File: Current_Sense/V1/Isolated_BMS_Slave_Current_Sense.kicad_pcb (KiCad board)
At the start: 2 copper layers, 107.6 x 62.2 mm, 140 parts, among them J202 649002227222, J301 649006227222, J302 649006227222, J401 Header_Male_Pin_2.54mm_1X2_,_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, J501 Header_Male_Pin_2.54mm_1X6_,_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, J502 Header_Male_Pin_2.54mm_1X3_,_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, SW501 PTS645SM43SMTR92, SW502 PTS645SM43SMTR92, U201 LM4040CYM3-4.1-TR, U202 PGA281AIPWR, U203 ADC141S626CIMM/NOPB, U301 SI8422AB-D-IS, U302 SN65HVD232DR, U401 PQMC3-D12-D15-S, U402 NCP1117LPST33T3G, U403 NCP1117ST50T3G, U404 NCP1117LPST33T3G, U501 STM32F446RE

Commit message: minor fix
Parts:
- added C210: 885012107018, Capacitors:C0805, B.Cu at (128.5, 91.7)
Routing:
- net 5VB: track 143.1 -> 145.7 mm
- net /STM32F446/PA3: track 49.5 -> 50.9 mm
- net /STM32F446/PA2: track 48.3 -> 49.1 mm
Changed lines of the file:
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@@
 (kicad_pcb (version 4) (host pcbnew 4.0.5+dfsg1-4)
   (general
-    (links 273)
+    (links 275)
     (no_connects 0)
-    (area 103.048999 60.884999 210.768001 123.265001)
+    (area 95.865647 23.000933 221.091788 157.954066)
     (thickness 1.6)
     (drawings 34)
-    (tracks 1007)
+    (tracks 1009)
     (zones 0)
-    (modules 140)
+    (modules 141)
     (nets 113)
   )
@@
   )
   (setup
-    (last_trace_width 0.254)
+    (last_trace_width 0.508)
     (user_trace_width 0.2032)
     (user_trace_width 0.254)
@@
     (visible_elements FFFFFF7F)
     (pcbplotparams
-      (layerselection 0x00030_80000001)
-      (usegerberextensions false)
+      (layerselection 0x010f0_80000001)
+      (usegerberextensions true)
       (excludeedgelayer true)
       (linewidth 0.100000)
       (plotframeref false)
-      (viasonmask false)
+      (viasonmask true)
       (mode 1)
       (useauxorigin false)
@@
       (outputformat 1)
       (mirror false)
-      (drillshape 1)
+      (drillshape 0)
       (scaleselection 1)
-      (outputdirectory ""))
+      (outputdirectory Gerber/))
   )
   (net 0 "")
@@
   (module Capacitors:C0805 (layer B.Cu)
     (at 131.064 91.712 90)
-    (fp_text reference C205 (at 0.78 -2.159 90) (layer B.SilkS)
+    (fp_text reference C205 (at -3.538 -0.127 90) (layer B.SilkS)
       (effects (font (size 1.27 1.27) (thickness 0.2032)) (justify mirror))
     )
@@
     (at 182.499 100.203)
     (fp_text reference F401 (at -0.254 -3.048) (layer F.SilkS)
-      (effects (font (size 1 1) (thickness 0.2032)))
+      (effects (font (size 1.27 1.27) (thickness 0.2032)))
     )
     (fp_text value 39511000440 (at 0 6.096) (layer F.Fab) hide
@@
     (at 151.511 76.581 90)
     (fp_text reference R404 (at 1.524 -2.032 90) (layer F.SilkS)
-      (effects (font (size 1.27 1.27) (thickness 0.254)))
+      (effects (font (size 1.27 1.27) (thickness 0.2032)))
     )
     (fp_text value RC0805JR-07470RL (at 1.73 2.33 90) (layer F.Fab) hide
@@
     (at 146.812 76.581 90)
     (fp_text reference R405 (at 1.397 -2.159 90) (layer F.SilkS)
-      (effects (font (size 1.27 1.27) (thickness 0.254)))
+      (effects (font (size 1.27 1.27) (thickness 0.2032)))
     )
     (fp_text value RC0805JR-07470RL (at 1.73 2.33 90) (layer F.Fab) hide
@@
   (module Connectors:Headers_2.54mm_1X6 (layer F.Cu)
     (at 111.633 96.266 270)
-    (fp_text reference J501 (at 4.14 -3.84 270) (layer F.SilkS)
-      (effects (font (size 2.54 2.54) (thickness 0.254)))
+    (fp_text reference J501 (at 12.446 -2.667 270) (layer F.SilkS)
+      (effects (font (size 1.27 1.27) (thickness 0.2032)))
     )
     (fp_text value Header_Male_Pin_2.54mm_1X6_,_Unshrouded (at -0.17 5.06 270) (layer F.Fab) hide
@@
   (module Connectors:Headers_2.54mm_1X2 (layer F.Cu)
     (at 149.352 66.04 270)
-    (fp_text reference J401 (at 3.38 -3.3 270) (layer F.SilkS)
-      (effects (font (size 2.54 2.54) (thickness 0.254)))
+    (fp_text reference J401 (at 3.048 2.54 450) (layer F.SilkS)
+      (effects (font (size 1.27 1.27) (thickness 0.2032)))
     )
     (fp_text value Header_Male_Pin_2.54mm_1X2_,_Unshrouded (at -0.13 5.58 270) (layer F.Fab) hide
@@
     )
   )
+  (module Capacitors:C0805 (layer B.Cu)
+    (at 128.524 91.694 90)
+    (fp_text reference C210 (at -3.429 0 90) (layer B.SilkS)
+      (effects (font (size 1.27 1.27) (thickness 0.2032)) (justify mirror))
+    )
+    (fp_text value 885012107018 (at 1.73 -2.33 90) (layer B.Fab) hide
+      (effects (font (size 1.27 1.27) (thickness 0.254)) (justify mirror))
+    )
+    (fp_line (start 0.6 1) (end 1.45 1) (layer B.SilkS) (width 0.254))
+    (fp_line (start 0.6 -1) (end 1.45 -1) (layer B.SilkS) (width 0.254))
+    (pad 1 smd rect (at 0 0 90) (size 1.4 1.5) (layers B.Cu B.Paste B.Mask)
+      (net 5 5VB))
+    (pad 2 smd rect (at 2.05 0 90) (size 1.4 1.5) (layers B.Cu B.Paste B.Mask)
+      (net 1 DGND))
+    (model Capacitors/C0805.wrl
+      (at (xyz 0.04 0.0005 0))
+      (scale (xyz 0.3937 0.3937 0.3937))
+      (rotate (xyz 0 0 0))
+    )
+  )
   (gr_text 3.3V (at 153.416 63.5) (layer F.SilkS)
     (effects (font (size 1.27 1.27) (thickness 0.2032)))
@@
   (segment (start 131.77 78.161) (end 131.699 78.232) (width 0.254) (layer F.Cu) (net 4))
   (via (at 131.699 78.232) (size 1.016) (drill 0.3302) (layers F.Cu B.Cu) (net 4))
+  (segment (start 131.064 91.712) (end 133.586 91.712) (width 0.508) (layer B.Cu) (net 5))
+  (segment (start 133.586 91.712) (end 133.604 91.694) (width 0.508) (layer B.Cu) (net 5))
+  (segment (start 128.524 91.694) (end 130.937 91.694) (width 0.508) (layer B.Cu) (net 5))
+  (segment (start 130.937 91.839) (end 131.064 91.712) (width 0.508) (layer B.Cu) (net 5))
   (segment (start 151.511 74.531) (end 153.525 74.531) (width 0.254) (layer F.Cu) (net 5))
   (segment (start 153.525 74.531) (end 156.21 77.216) (width 0.254) (layer F.Cu) (net 5))
@@
   (segment (start 130.937 93.19259) (end 131.318 93.19259) (width 0.2032) (layer F.Cu) (net 5))
   (segment (start 131.318 93.19259) (end 133.45159 93.19259) (width 0.2032) (layer F.Cu) (net 5))
-  (segment (start 131.064 91.712) (end 133.586 91.712) (width 0.2032) (layer B.Cu) (net 5))
-  (segment (start 133.586 91.712) (end 133.604 91.694) (width 0.2032) (layer B.Cu) (net 5))
   (segment (start 133.604 93.345) (end 133.604 91.694) (width 0.2032) (layer B.Cu) (net 5))
   (segment (start 133.45159 93.19259) (end 133.604 93.345) (width 0.2032) (layer F.Cu) (net 5))
@@
   (segment (start 116.223 91.313) (end 118.981 91.313) (width 0.508) (layer F.Cu) (net 31))
   (segment (start 118.981 91.313) (end 118.999 91.331) (width 0.508) (layer F.Cu) (net 31))
+  (segment (start 148.971 105.791) (end 148.971 108.458) (width 0.2032) (layer F.Cu) (net 32))
+  (segment (start 148.971 108.458) (end 152.908 112.395) (width 0.2032) (layer F.Cu) (net 32))
+  (segment (start 152.908 112.395) (end 152.908 120.269) (width 0.2032) (layer F.Cu) (net 32))
+  (segment (start 152.908 120.269) (end 151.765 121.412) (width 0.2032) (layer F.Cu) (net 32))
+  (segment (start 151.765 121.412) (end 126.873 121.412) (width 0.2032) (layer F.Cu) (net 32))
+  (segment (start 126.873 121.412) (end 125.476 120.015) (width 0.2032) (layer F.Cu) (net 32))
   (segment (start 125.476 120.015) (end 122.936 120.015) (width 0.2032) (layer F.Cu) (net 32))
   (segment (start 122.936 120.015) (end 121.031 120.015) (width 0.2032) (layer F.Cu) (net 32))
   (segment (start 121.031 120.015) (end 122.936 120.015) (width 0.254) (layer B.Cu) (net 32))
   (via (at 122.936 120.015) (size 1.016) (drill 0.3302) (layers F.Cu B.Cu) (net 32))
-  (segment (start 148.971 105.791) (end 148.971 108.458) (width 0.2032) (layer F.Cu) (net 32))
-  (segment (start 148.971 108.458) (end 152.171411 111.658411) (width 0.2032) (layer F.Cu) (net 32))
-  (segment (start 152.171411 111.658411) (end 152.171411 119.735589) (width 0.2032) (layer F.Cu) (net 32))
-  (segment (start 152.171411 119.735589) (end 150.622 121.285) (width 0.2032) (layer F.Cu) (net 32))
-  (segment (start 150.622 121.285) (end 126.746 121.285) (width 0.2032) (layer F.Cu) (net 32))
-  (segment (start 126.746 121.285) (end 125.476 120.015) (width 0.2032) (layer F.Cu) (net 32))
   (segment (start 186.436 78.74) (end 188.087 78.74) (width 0.508) (layer B.Cu) (net 33))
   (segment (start 188.087 78.74) (end 188.341 78.994) (width 0.508) (layer B.Cu) (net 33))
@@
   (segment (start 111.633 91.313) (end 114.173 91.313) (width 0.508) (layer F.Cu) (net 66))
   (segment (start 146.821 107.941) (end 146.821 108.8942) (width 0.2032) (layer F.Cu) (net 67))
-  (segment (start 151.765001 113.838201) (end 151.765001 119.506999) (width 0.2032) (layer F.Cu) (net 67))
-  (segment (start 146.821 108.8942) (end 151.765001 113.838201) (width 0.2032) (layer F.Cu) (net 67))
-  (segment (start 151.765001 119.506999) (end 150.495 120.777) (width 0.2032) (layer F.Cu) (net 67))
-  (segment (start 150.495 120.777) (end 127.254 120.777) (width 0.2032) (layer F.Cu) (net 67))
-  (segment (start 127.254 120.777) (end 123.952 117.475) (width 0.2032) (layer F.Cu) (net 67))
+  (segment (start 146.821 108.8942) (end 152.146 114.2192) (width 0.2032) (layer F.Cu) (net 67))
+  (segment (start 152.146 114.2192) (end 152.146 119.888) (width 0.2032) (layer F.Cu) (net 67))
+  (segment (start 152.146 119.888) (end 151.13 120.904) (width 0.2032) (layer F.Cu) (net 67))
+  (segment (start 151.13 120.904) (end 127.381 120.904) (width 0.2032) (layer F.Cu) (net 67))
+  (segment (start 127.381 120.904) (end 123.952 117.475) (width 0.2032) (layer F.Cu) (net 67))
   (segment (start 123.952 117.475) (end 118.999 117.475) (width 0.2032) (layer F.Cu) (net 67))
   (segment (start 133.302 77.511) (end 137.543 77.511) (width 0.254) (layer F.Cu) (net 72))
@@
     (polygon
       (pts
-        (xy 204.47 75.311) (xy 204.47 60.96) (xy 107.95 60.96) (xy 107.95 123.19) (xy 162.56 123.19)
+        (xy 203.708 75.311) (xy 203.708 60.96) (xy 107.95 60.96) (xy 107.95 123.19) (xy 162.56 123.19)
         (xy 162.56 76.454) (xy 163.83 75.311)
       )

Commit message: Add Eclipse Logo, generate Gerber
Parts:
- added G***: LOGO, Logo:Eclipse_logo_small, B.Cu at (123.0, 68.5)
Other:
- board text added: "Christian Daigneault-St-Arnaud (c) 2017 - Eclipse X BMS - Current Sense V1"

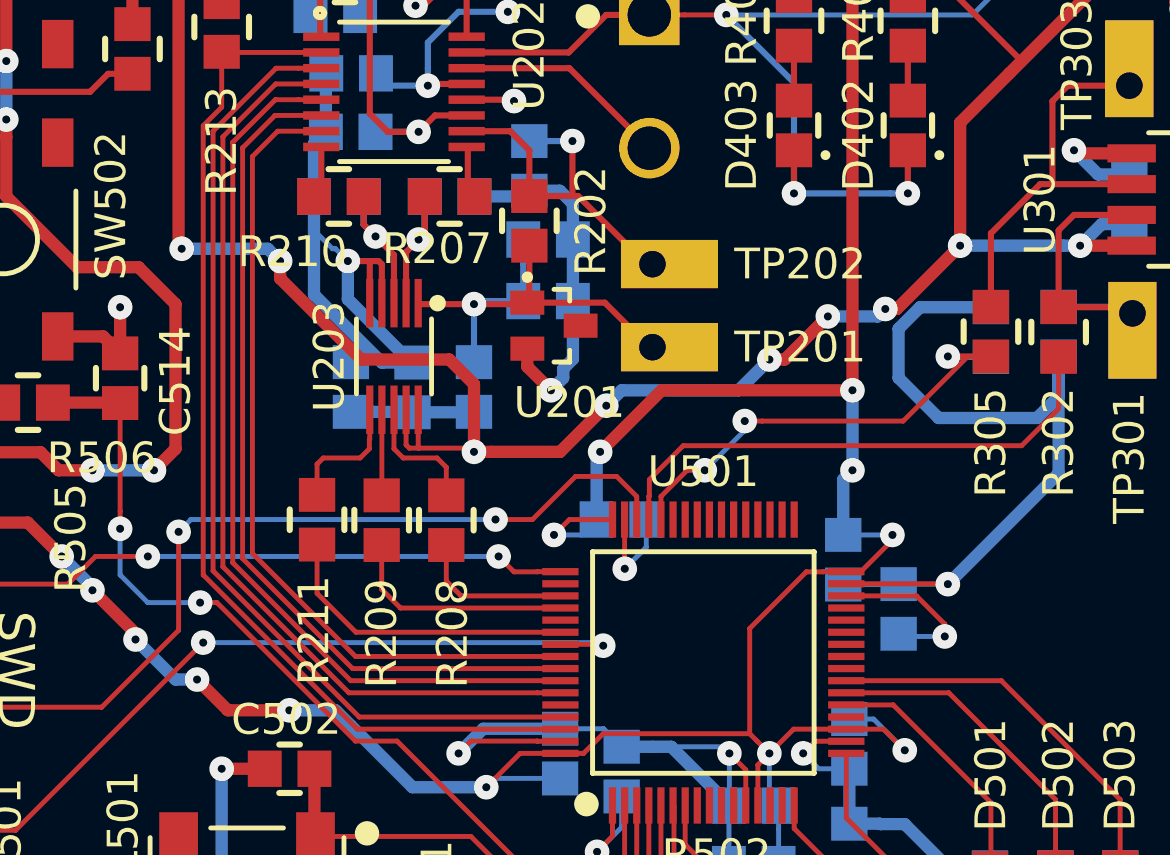
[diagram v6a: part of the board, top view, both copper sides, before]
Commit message: Move CAN to CAN2, Generate GERBER
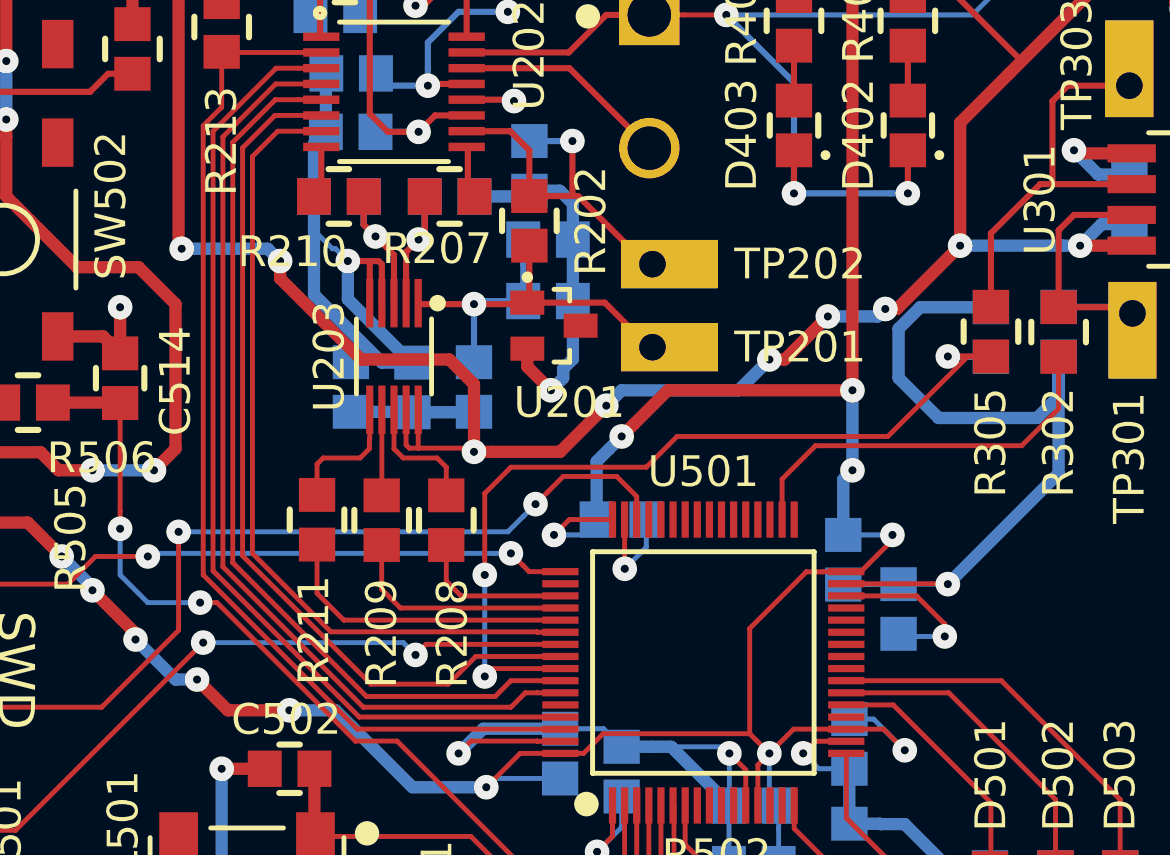
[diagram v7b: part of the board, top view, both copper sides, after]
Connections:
- C308 pad 1: /STM32F446/PA11 -> /STM32F446/PB5
- R302 pad 1: /STM32F446/PA12 -> /STM32F446/PB13
- R305 pad 2: /STM32F446/PA11 -> /STM32F446/PB5
- U501 pad 53: /STM32F446/PC12 -> /Current Sense/CS
- U501 pad 54: /Current Sense/CS -> /Current Sense/G0
- U501 pad 56: /Current Sense/G0 -> /Current Sense/G1
- U501 pad 57: /Current Sense/G1 -> /STM32F446/PB5
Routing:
- net /STM32F446/PB5: track 0.00 -> 37.6 mm, vias 0 -> 3
- net /STM32F446/PA12: track 21.9 -> 0.00 mm
- net /STM32F446/PA11: track 20.8 -> 0.00 mm, vias 3 -> 0
- net /STM32F446/PB13: track 0.00 -> 16.4 mm
- net /STM32F446/SWO: track 32.4 -> 29.1 mm
- net /Current Sense/G1: track 35.8 -> 36.4 mm
- net /Current Sense/G2: track 37.3 -> 37.8 mm
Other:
- net class Default: via_dia 1.016 -> 0.762; via_drill 0.3302 -> 0.254
- rule via_min_drill: 0.3302 -> 0.254
- rule via_min_size: 1.016 -> 0.762

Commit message: Fix funky trace, Generate GERBER
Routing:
- net /STM32F446/PB5: track 37.6 -> 38.8 mm
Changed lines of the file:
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@@
     (links 275)
     (no_connects 0)
-    (area 103.048999 60.884999 210.768001 123.265001)
+    (area 95.865647 23.000933 221.091788 157.954066)
     (thickness 1.6)
     (drawings 35)
@@
   (segment (start 151.511 76.581) (end 151.511 78.849) (width 0.254) (layer F.Cu) (net 110))
   (segment (start 146.812 76.581) (end 146.812 78.849) (width 0.254) (layer F.Cu) (net 111))
+  (segment (start 154.94 89.408) (end 154.94 91.3765) (width 0.2032) (layer F.Cu) (net 112))
+  (segment (start 154.94 91.3765) (end 153.6065 92.71) (width 0.2032) (layer F.Cu) (net 112))
+  (segment (start 153.6065 92.71) (end 141.986 92.71) (width 0.2032) (layer F.Cu) (net 112))
+  (segment (start 141.986 92.71) (end 140.716 93.98) (width 0.2032) (layer F.Cu) (net 112))
+  (segment (start 140.716 93.98) (end 135.128 93.98) (width 0.2032) (layer F.Cu) (net 112))
+  (segment (start 135.128 93.98) (end 134.0485 95.0595) (width 0.2032) (layer F.Cu) (net 112))
+  (segment (start 134.0485 95.0595) (end 134.0485 97.706586) (width 0.2032) (layer F.Cu) (net 112))
+  (segment (start 134.0485 97.706586) (end 134.0485 98.425006) (width 0.2032) (layer F.Cu) (net 112))
   (segment (start 137.171 102.291) (end 134.373499 102.291) (width 0.2032) (layer F.Cu) (net 112))
   (via (at 134.0485 102.615999) (size 1.016) (drill 0.3302) (layers F.Cu B.Cu) (net 112))
   (segment (start 134.0485 98.425006) (end 134.0485 102.615999) (width 0.2032) (layer B.Cu) (net 112))
   (segment (start 134.373499 102.291) (end 134.0485 102.615999) (width 0.2032) (layer F.Cu) (net 112))
-  (segment (start 134.0485 97.706586) (end 134.0485 98.425006) (width 0.2032) (layer F.Cu) (net 112))
-  (segment (start 134.0485 95.0595) (end 134.0485 97.706586) (width 0.2032) (layer F.Cu) (net 112))
-  (segment (start 140.716 93.98) (end 135.128 93.98) (width 0.2032) (layer F.Cu) (net 112))
-  (segment (start 150.6848 92.71) (end 141.986 92.71) (width 0.2032) (layer F.Cu) (net 112))
-  (segment (start 153.9868 89.408) (end 150.6848 92.71) (width 0.2032) (layer F.Cu) (net 112))
-  (segment (start 154.94 89.408) (end 153.9868 89.408) (width 0.2032) (layer F.Cu) (net 112))
   (via (at 134.0485 98.425006) (size 1.016) (drill 0.3302) (layers F.Cu B.Cu) (net 112))
-  (segment (start 135.128 93.98) (end 134.0485 95.0595) (width 0.2032) (layer F.Cu) (net 112))
-  (segment (start 141.986 92.71) (end 140.716 93.98) (width 0.2032) (layer F.Cu) (net 112))
   (via (at 153.162 89.408) (size 1.016) (drill 0.3302) (layers F.Cu B.Cu) (net 112))
   (segment (start 153.162 89.408) (end 154.94 89.408) (width 0.254) (layer F.Cu) (net 112))
